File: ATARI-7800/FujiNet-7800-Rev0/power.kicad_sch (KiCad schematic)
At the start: 15 parts, among them Q2 AO3401A, U10 AP63203WU, U11 AP2112K-3.3

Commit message: ATARI-7800 Rev0: add the VBUS pull-down (R24 4.7k) against SS34 reverse leakage
Q2's gate is VBUS, which only the 69k CP2102N sense divider pulled down.
With the console powering the cart the SS34 is reverse-biased and leaks
into VBUS (0.5 mA max at 25 C); at >= 100 uA the AO3401A turns off and the
console feeds +5V through the body diode, ~0.7 V down, under the 74HCT /
SRAM 4.5 V minimum.  R24 4.7k VBUS-GND (0603WAF4701T5E, C23162) holds VGS
beyond -2.7 V up to 500 uA; same fix as NES Rev0 R22, SMS Rev0 and 2600
Rev1 R_VBPD.

- design.py: declared after every other resistor (no ref changes).
- power sheet: drawn with the NES Rev0 function (NES_FIRST gains R: 22).
- ERC 0, netlist parity 116 nets, check_nets 379/379, check_glue 4096/4096;
  BOM 103 fitted parts; schematic PDF regenerated; README power section.

Co-Authored-By: Claude Opus 5.5 <noreply@anthropic.com>
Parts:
- added R24: 4.7k, FujiNet-7800:R_0603_1608Metric, symbol Device:R
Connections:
- net GND: now also R24.2
- net VBUS: now also R24.1
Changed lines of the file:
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@@
+	)
+	(symbol
+		(lib_id "Device:R")
+		(at 121.92 135.89 0)
+		(unit 1)
+		(exclude_from_sim no)
+		(in_bom yes)
+		(on_board yes)
+		(dnp no)
+		(property "Reference" "R24"
+			(at 124.206 134.62 0)
+			(effects
+				(font
+					(size 1.27 1.27)
+				)
+				(justify left)
+			)
+		)
+		(property "Value" "4.7k"
+			(at 124.206 137.16 0)
+			(effects
+				(font
+					(size 1.27 1.27)
+				)
+				(justify left)
+			)
+		)
+		(property "Footprint" "FujiNet-7800:R_0603_1608Metric"
+			(at 121.92 135.89 0)
+			(effects
+				(font
+					(size 1.27 1.27)
+				)
+				(hide yes)
+			)
+		)
+		(property "Datasheet" ""
+			(at 121.92 135.89 0)
+			(effects
+				(font
+					(size 1.27 1.27)
+				)
+				(hide yes)
+			)
+		)
+		(property "Description" "P-FET gate pull-down against the SS34 reverse leakage"
+			(at 121.92 135.89 0)
+			(effects
+				(font
+					(size 1.27 1.27)
+				)
+				(hide yes)
+			)
+		)
+		(property "MPN" "0603WAF4701T5E"
+			(at 121.92 135.89 0)
+			(effects
+				(font
+					(size 1.27 1.27)
+				)
+				(hide yes)
+			)
+		)
+		(property "LCSC" "C23162"
+			(at 121.92 135.89 0)
+			(effects
+				(font
+					(size 1.27 1.27)
+				)
+				(hide yes)
+			)
+		)
+		(pin "1"
+		)
+		(pin "2"
+		)
+		(instances
+			(project "FujiNet-7800-Rev0"
+				(path "/ff394b2b-0001-5468-a47f-d8dd41a97fc7/113877c5-6a44-5bff-9a74-179e8fd72159"
+					(reference "R24")
+					(unit 1)
+				)
+			)
+		)
 	)
 	(symbol
@@
 	)
 	(symbol
+		(lib_id "power:GND")
+		(at 121.92 139.7 0)
+		(unit 1)
+		(exclude_from_sim no)
+		(in_bom no)
+		(on_board no)
+		(dnp no)
+		(property "Reference" "#PWR102"
+			(at 121.92 146.05 0)
+			(effects
+				(font
+					(size 1.27 1.27)
+				)
+				(hide yes)
+			)
+		)
+		(property "Value" "GND"
+			(at 121.92 143.51 0)
+			(effects
+				(font
+					(size 1.27 1.27)
+				)
+			)
+		)
+		(property "Footprint" ""
+			(at 121.92 139.7 0)
+			(effects
+				(font
+					(size 1.27 1.27)
+				)
+				(hide yes)
+			)
+		)
+		(property "Datasheet" ""
+			(at 121.92 139.7 0)
+			(effects
+				(font
+					(size 1.27 1.27)
+				)
+				(hide yes)
+			)
+		)
+		(property "Description" ""
+			(at 121.92 139.7 0)
+			(effects
+				(font
+					(size 1.27 1.27)
+				)
+				(hide yes)
+			)
+		)
+		(pin "1"
+		)
+		(instances
+			(project "FujiNet-7800-Rev0"
+				(path "/ff394b2b-0001-5468-a47f-d8dd41a97fc7/113877c5-6a44-5bff-9a74-179e8fd72159"
+					(reference "#PWR102")
+					(unit 1)
+				)
+			)
+		)
+	)
+	(symbol
 		(lib_id "power:+5V")
 		(at 172.72 104.14 0)
@@
 		(on_board no)
 		(dnp no)
-		(property "Reference" "#PWR102"
+		(property "Reference" "#PWR103"
 			(at 172.72 97.79 0)
 			(effects
@@
 			(project "FujiNet-7800-Rev0"
 				(path "/ff394b2b-0001-5468-a47f-d8dd41a97fc7/113877c5-6a44-5bff-9a74-179e8fd72159"
-					(reference "#PWR102")
+					(reference "#PWR103")
 					(unit 1)
 				)
@@
 		(on_board no)
 		(dnp no)
-		(property "Reference" "#PWR103"
+		(property "Reference" "#PWR104"
 			(at 182.88 118.11 0)
 			(effects
@@
 			(project "FujiNet-7800-Rev0"
 				(path "/ff394b2b-0001-5468-a47f-d8dd41a97fc7/113877c5-6a44-5bff-9a74-179e8fd72159"
-					(reference "#PWR103")
+					(reference "#PWR104")
 					(unit 1)
 				)
@@
 		(on_board no)
 		(dnp no)
-		(property "Reference" "#PWR104"
+		(property "Reference" "#PWR105"
 			(at 193.04 118.11 0)
 			(effects
@@
 			(project "FujiNet-7800-Rev0"
 				(path "/ff394b2b-0001-5468-a47f-d8dd41a97fc7/113877c5-6a44-5bff-9a74-179e8fd72159"
-					(reference "#PWR104")
+					(reference "#PWR105")
 					(unit 1)
 				)
@@
 		(on_board no)
 		(dnp no)
-		(property "Reference" "#PWR105"
+		(property "Reference" "#PWR106"
 			(at 203.2 118.11 0)
 			(effects
@@
 			(project "FujiNet-7800-Rev0"
 				(path "/ff394b2b-0001-5468-a47f-d8dd41a97fc7/113877c5-6a44-5bff-9a74-179e8fd72159"
-					(reference "#PWR105")
+					(reference "#PWR106")
 					(unit 1)
 				)
@@
 		(on_board no)
 		(dnp no)
-		(property "Reference" "#PWR106"
+		(property "Reference" "#PWR107"
 			(at 213.36 118.11 0)
 			(effects
@@
 			(project "FujiNet-7800-Rev0"
 				(path "/ff394b2b-0001-5468-a47f-d8dd41a97fc7/113877c5-6a44-5bff-9a74-179e8fd72159"
-					(reference "#PWR106")
+					(reference "#PWR107")
 					(unit 1)
 				)
@@
 		(on_board no)
 		(dnp no)
-		(property "Reference" "#PWR107"
+		(property "Reference" "#PWR108"
 			(at 246.38 120.65 0)
 			(effects
@@
 			(project "FujiNet-7800-Rev0"
 				(path "/ff394b2b-0001-5468-a47f-d8dd41a97fc7/113877c5-6a44-5bff-9a74-179e8fd72159"
-					(reference "#PWR107")
+					(reference "#PWR108")
 					(unit 1)
 				)
@@
 		(on_board no)
 		(dnp no)
-		(property "Reference" "#PWR108"
+		(property "Reference" "#PWR109"
 			(at 288.29 97.79 0)
 			(effects
@@
 			(project "FujiNet-7800-Rev0"
 				(path "/ff394b2b-0001-5468-a47f-d8dd41a97fc7/113877c5-6a44-5bff-9a74-179e8fd72159"
-					(reference "#PWR108")
+					(reference "#PWR109")
 					(unit 1)
 				)
@@
 		(on_board no)
 		(dnp no)
-		(property "Reference" "#PWR109"
+		(property "Reference" "#PWR110"
 			(at 293.37 118.11 0)
 			(effects
@@
 			(project "FujiNet-7800-Rev0"
 				(path "/ff394b2b-0001-5468-a47f-d8dd41a97fc7/113877c5-6a44-5bff-9a74-179e8fd72159"
-					(reference "#PWR109")
+					(reference "#PWR110")
 					(unit 1)
 				)
@@
 		(on_board no)
 		(dnp no)
-		(property "Reference" "#PWR110"
+		(property "Reference" "#PWR111"
 			(at 303.53 118.11 0)
 			(effects
@@
 			(project "FujiNet-7800-Rev0"
 				(path "/ff394b2b-0001-5468-a47f-d8dd41a97fc7/113877c5-6a44-5bff-9a74-179e8fd72159"
-					(reference "#PWR110")
+					(reference "#PWR111")
 					(unit 1)
 				)
@@
 		(on_board no)
 		(dnp no)
-		(property "Reference" "#PWR111"
+		(property "Reference" "#PWR112"
 			(at 223.52 168.91 0)
 			(effects
@@
 			(project "FujiNet-7800-Rev0"
 				(path "/ff394b2b-0001-5468-a47f-d8dd41a97fc7/113877c5-6a44-5bff-9a74-179e8fd72159"
-					(reference "#PWR111")
+					(reference "#PWR112")
 					(unit 1)
 				)
@@
 		(on_board no)
 		(dnp no)
-		(property "Reference" "#PWR112"
+		(property "Reference" "#PWR113"
 			(at 238.76 171.45 0)
 			(effects
@@
 			(project "FujiNet-7800-Rev0"
 				(path "/ff394b2b-0001-5468-a47f-d8dd41a97fc7/113877c5-6a44-5bff-9a74-179e8fd72159"
-					(reference "#PWR112")
+					(reference "#PWR113")
 					(unit 1)
 				)
@@
 		(on_board no)
 		(dnp no)
-		(property "Reference" "#PWR113"
+		(property "Reference" "#PWR114"
 			(at 254 168.91 0)
 			(effects
@@
 			(project "FujiNet-7800-Rev0"
 				(path "/ff394b2b-0001-5468-a47f-d8dd41a97fc7/113877c5-6a44-5bff-9a74-179e8fd72159"
-					(reference "#PWR113")
+					(reference "#PWR114")
 					(unit 1)
 				)
@@
 		(on_board no)
 		(dnp no)
-		(property "Reference" "#PWR114"
+		(property "Reference" "#PWR115"
 			(at 259.08 148.59 0)
 			(effects
@@
 			(project "FujiNet-7800-Rev0"
 				(path "/ff394b2b-0001-5468-a47f-d8dd41a97fc7/113877c5-6a44-5bff-9a74-179e8fd72159"
-					(reference "#PWR114")
+					(reference "#PWR115")
 					(unit 1)
 				)
@@
 		(pts
 			(xy 111.76 132.08)
+			(xy 121.92 132.08)
+		)
+		(stroke
+			(width 0)
+			(type default)
+		)
+	)
+	(wire
+		(pts
+			(xy 121.92 132.08)
 			(xy 132.08 132.08)
 		)
@@
 	)
 	(junction
+		(at 121.92 132.08)
+		(diameter 0)
+		(color 0 0 0 0)
+	)
+	(junction

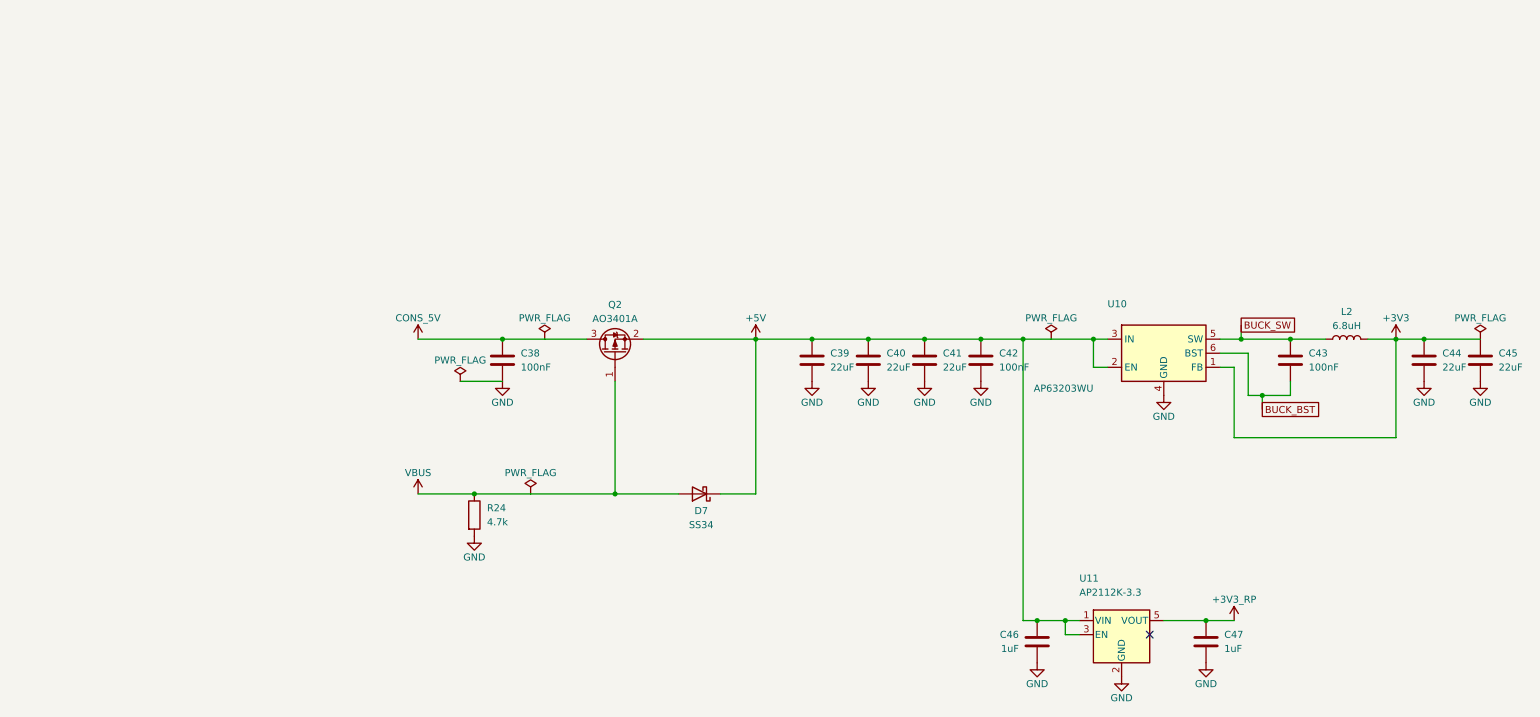
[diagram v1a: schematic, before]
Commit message: ATARI-7800 Rev0: fix the edge, audit the circuit, redraw from the slot, place the board
Edge (board-killer in the schematic-only footprint): the 7800 edge has 18
positions at 2.54 mm with key slots at 3 and 16 for the console's plastic
keys. Pins 1, 2, 15, 16 (and 32, 31, 18, 17) sat one pitch inward, on the
key positions, with no slots and a 42.6 mm tab. tools/edge_geom.py now holds
the geometry (47.0 mm tab, slots centred on +-16.51, 2.4 x 10 mm);
tools/audit/edge_orientation.py checks it against Otaku-flash, tdididit's
boards, the a78-devcart gerbers and this repo's working FujiPlusCart
prototype gerbers (faces and power fingers).

Circuit (console research: Atari C025231 schematic, GCC1702B MARIA spec):
- 4.7k pull-downs on ROM_EN / RAM_EN / A8MASK (RP2350-E9)
- 1k at the /HALT finger (MARIA's HALT is a weak MOS output)
- 10 uF at the console 5V finger; bring-up test pads
- TS-1187A buttons and WS2812C-2020-V1 (the TL3342 and WS2812B-2020
  had 5 in stock at JLC); manufacturer fields for PCBWay
No glue change: R/W is pulled up during MARIA DMA, and the console gates
A15/A14/A12 low while its BIOS is mapped, so CARTSEL never fights it.

Schematic: SMS Rev0's hierarchy (wired root block diagram, hierarchical
labels, netlist parity); sheets in flow order from the slot; the glue
redrawn as a left-to-right gate-depth diagram; references renumbered
from the slot. ERC 0, check_nets 383/383, check_glue 4096/4096.

Board (not yet routed): SMS Rev0's 6-layer pipeline ported. A 72.4 x 115 mm
outline: the stock T-bar width on a 47 x 16.5 mm tab, with the key slots
cut in. Placement variant A (RP over the address fingers, SRAM over the
data fingers): unrouted DRC 0 errors, parity 0, check_vias 0. Shell:
case/FujiNet-7800-Shell.scad. README still describes the old board.

Co-Authored-By: Claude Opus 5.5 <noreply@anthropic.com>
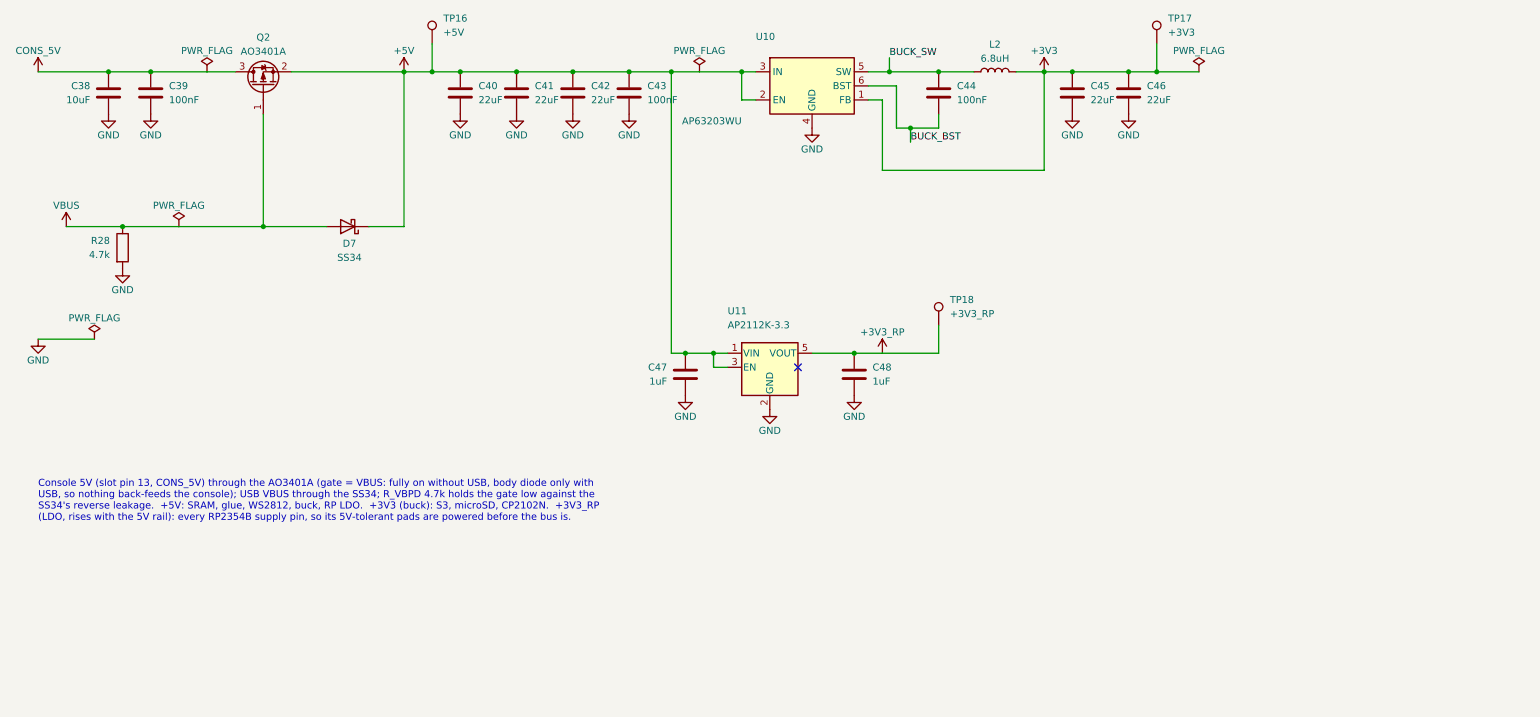
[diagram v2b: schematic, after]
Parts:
- removed R24: 4.7k, FujiNet-7800:R_0603_1608Metric, symbol Device:R
- added C48: 1uF, FujiNet-7800:C_0603_1608Metric, symbol Device:C
- added R28: 4.7k, FujiNet-7800:R_0603_1608Metric, symbol Device:R
- added TP16: +5V, FujiNet-7800:TestPoint_Pad_D1.5mm, symbol Connector:TestPoint
- added TP17: +3V3, FujiNet-7800:TestPoint_Pad_D1.5mm, symbol Connector:TestPoint
- added TP18: +3V3_RP, FujiNet-7800:TestPoint_Pad_D1.5mm, symbol Connector:TestPoint
- C38: value 100nF -> 10uF; LCSC C14663 -> C19702; MPN CC0603KRX7R9BB104 -> CL10A106KP8NNNC
- C39, C44: value 22uF -> 100nF; footprint FujiNet-7800:C_0805_2012Metric -> FujiNet-7800:C_0603_1608Metric; LCSC C45783 -> C14663; MPN CL21A226MAQNNNE -> CC0603KRX7R9BB104
- C42: value 100nF -> 22uF; footprint FujiNet-7800:C_0603_1608Metric -> FujiNet-7800:C_0805_2012Metric; LCSC C14663 -> C45783; MPN CC0603KRX7R9BB104 -> CL21A226MAQNNNE
- C46: value 1uF -> 22uF; footprint FujiNet-7800:C_0603_1608Metric -> FujiNet-7800:C_0805_2012Metric; LCSC C15849 -> C45783; MPN CL10A105KB8NNNC -> CL21A226MAQNNNE
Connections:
- net +3V3: now also C46.1, TP17.1; no longer C44.1
- net +3V3_RP: now also C48.1, TP18.1; no longer C47.1
- net +5V: now also C43.1, C47.1, TP16.1; no longer C39.1, C46.1
- net BUCK_BST: now also C44.2; no longer C43.2
- net BUCK_SW: now also C44.1; no longer C43.1
- net CONS_5V: now also C39.1
- net GND: now also C43.2, C48.2, R28.2; no longer C44.2
- net VBUS: now also R28.1
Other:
- note added: "Console 5V (slot pin 13, CONS_5V) through the AO3401A (gate = VBUS: fully on without USB, body diode only with USB, so nothing back-feeds the console); USB VBUS through the SS34; R_VBPD 4.7k holds the gate low against the SS34's reverse leakage. +5V: SRAM, glue, WS2812, buck, RP LDO. +3V3 (buck): S3, microSD, CP2102N. +3V3_RP (LDO, rises with the 5V rail): every RP2354B supply pin, so its 5V-tole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"
- moved on the sheet: C38, C39, C40, C41, C42, C43, C44, C45, C46, C47, D7, L2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
